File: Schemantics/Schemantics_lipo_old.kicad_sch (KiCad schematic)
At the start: 23 parts, among them IC1 MCP73831T-2ACI_OT, IC2 MCP1725-3302E_MC, J1 Conn_01x04, J2 Conn_01x02, Q1 BC547, U1 ESP32-WROOM-32D

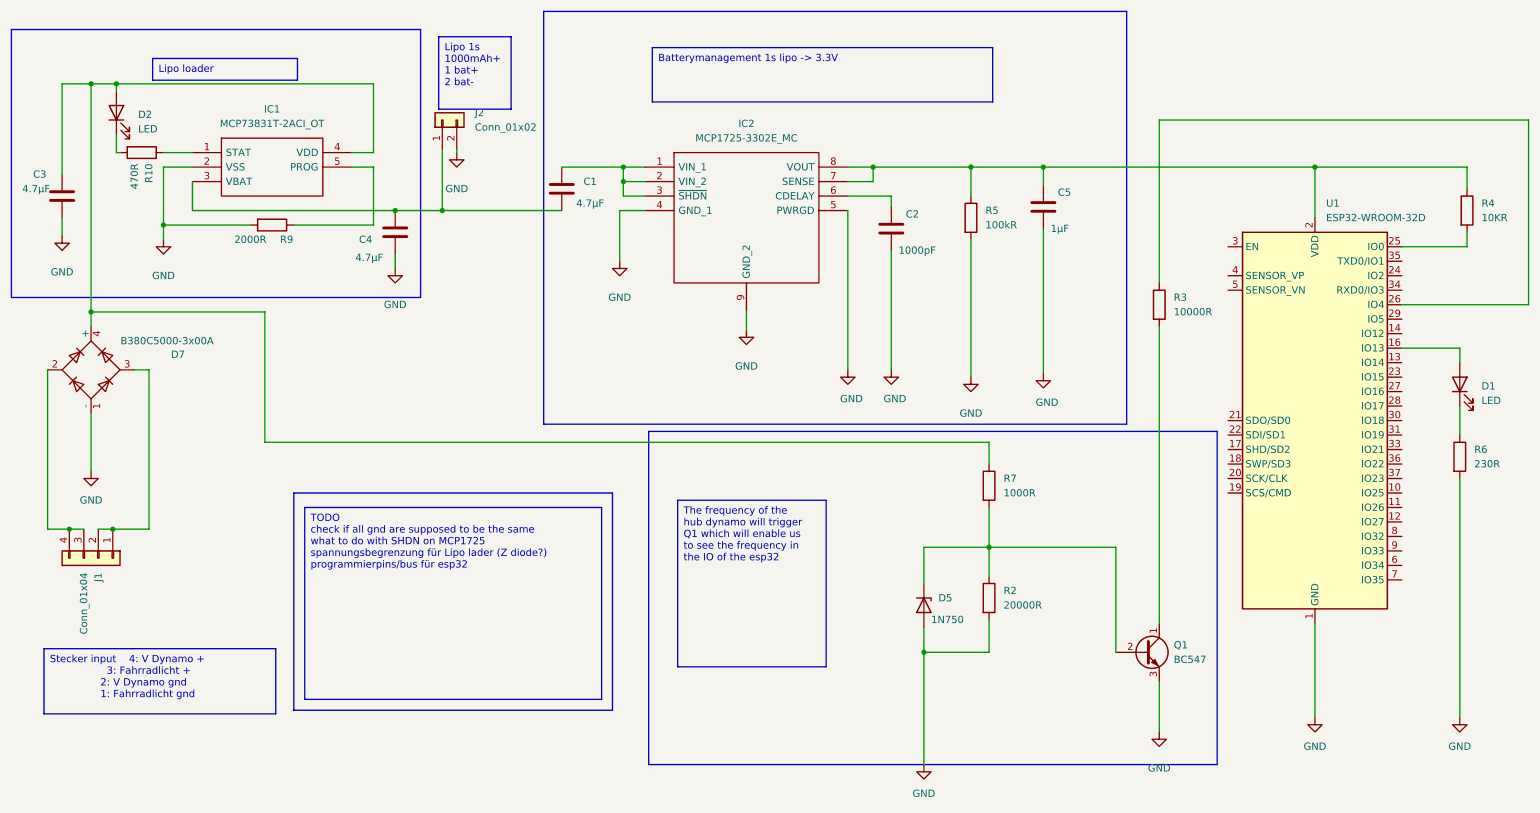
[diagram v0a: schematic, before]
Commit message: added Lipo loader and BMS for the 3.3V powered mC
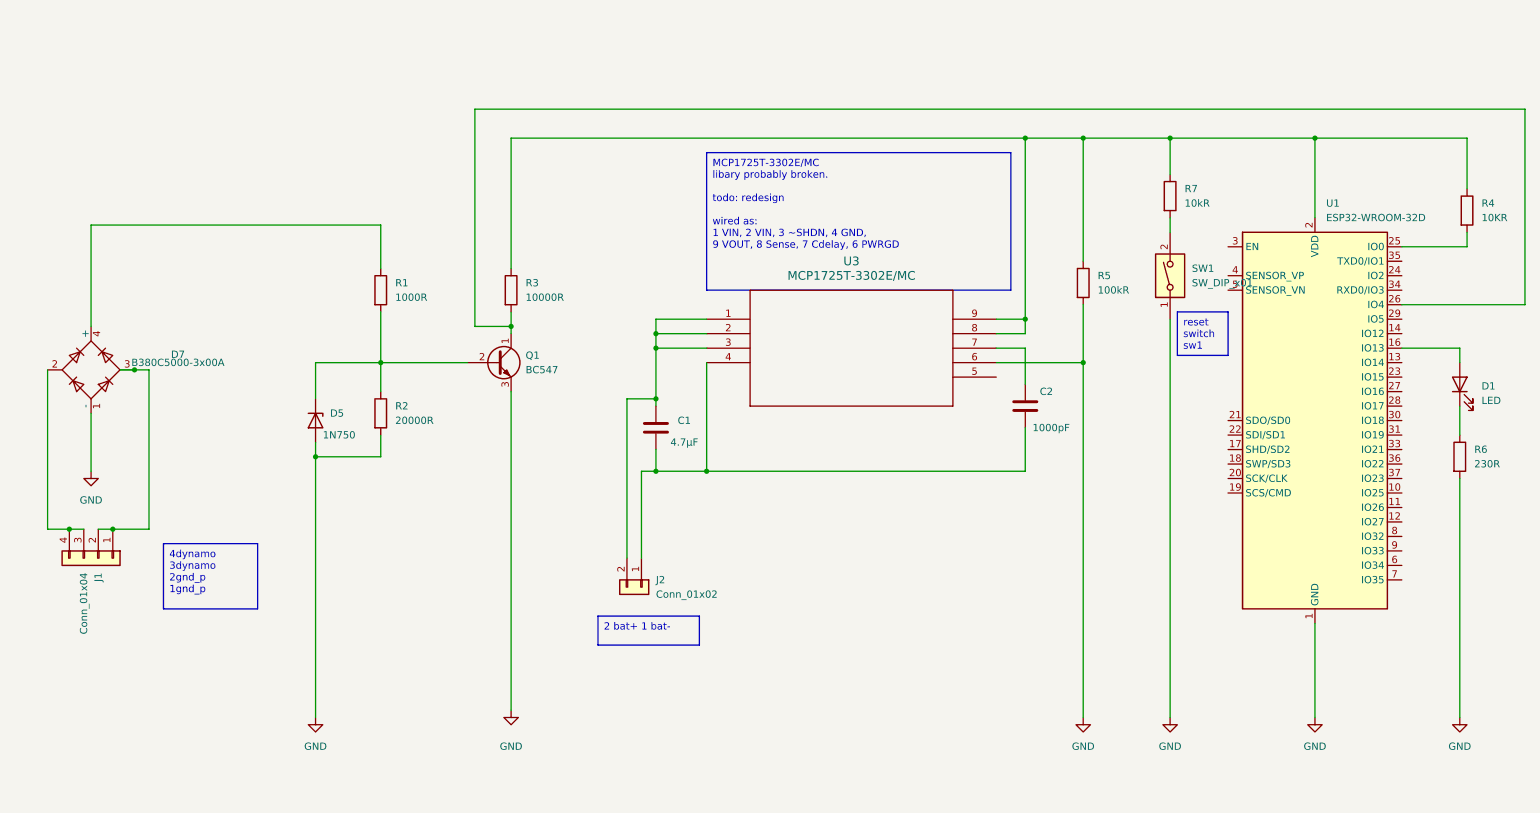
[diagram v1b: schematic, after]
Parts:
- removed C3, C4: 4.7μF, Capacitor_THT:C_Rect_L16.5mm_W4.7mm_P15.00mm_MKT, symbol Device:C
- removed C5: 1µF, Capacitor_THT:C_Rect_L16.5mm_W4.7mm_P15.00mm_MKT, symbol Device:C
- removed D2: LED, symbol Device:LED
- removed IC1: MCP73831T-2ACI_OT, SOT95P270X145-5N, symbol MCP73831T-2ACI_OT lib:MCP73831T-2ACI_OT
- removed IC2: MCP1725-3302E_MC, SON50P300X200X100-9N-D, symbol MCP1725-3302E/MC lib:MCP1725-3302E_MC
- removed R10: 470R, symbol Device:R
- removed R9: 2000R, Resistor_SMD:R_0805_2012Metric_Pad1.20x1.40mm_HandSolder, symbol Device:R
- added R1: 1000R, Resistor_SMD:R_0805_2012Metric_Pad1.20x1.40mm_HandSolder, symbol Device:R
- added SW1: SW_DIP_x01, symbol Switch:SW_DIP_x01
- added U3: MCP1725T-3302E/MC, DFN8_2x3MC_MCH, symbol test:MCP1725T-3302E_MC
- R7: value 1000R -> 10kR; footprint Resistor_SMD:R_0805_2012Metric_Pad1.20x1.40mm_HandSolder -> (none)
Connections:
- net GND: now also SW1.1, U3.6; no longer C2.2, J2.2 (Pin_2)
- net at C1.2, J2.1 (Pin_1): now also C2.2, U3.4
- net at D7.4 (+): now also R1.1; no longer R7.1
- net at C1.1: now also J2.2 (Pin_2), U3.1, U3.2, U3.3
- net at C2.1: now also U3.7
- net at R4.1, R5.1, U1.2 (VDD): now also R3.1, R7.1, U3.8, U3.9
- net at Q1.1 (C), R3.2: now also U1.26 (IO4)
- net at D5.1 (K), Q1.2 (B), R2.1: now also R1.2; no longer R7.2
- new net: R7.2, SW1.2
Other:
- moved on the sheet: D5, Q1, R2, R3
